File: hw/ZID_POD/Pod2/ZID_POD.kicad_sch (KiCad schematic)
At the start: 2 parts, among them J1 Z80-POD

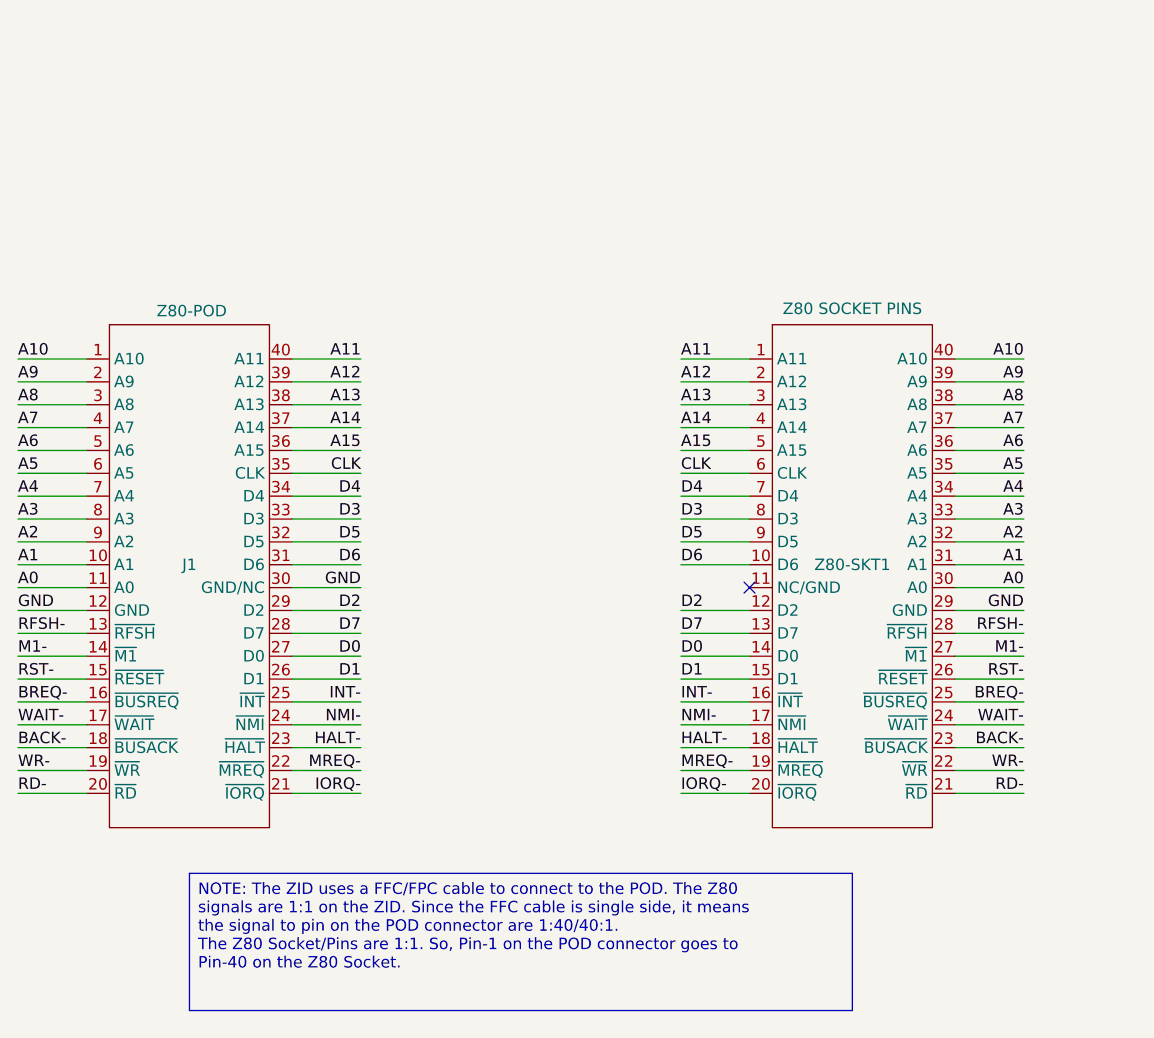
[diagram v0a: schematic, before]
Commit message: Change ZID,POD,ExpBP connector to SIP
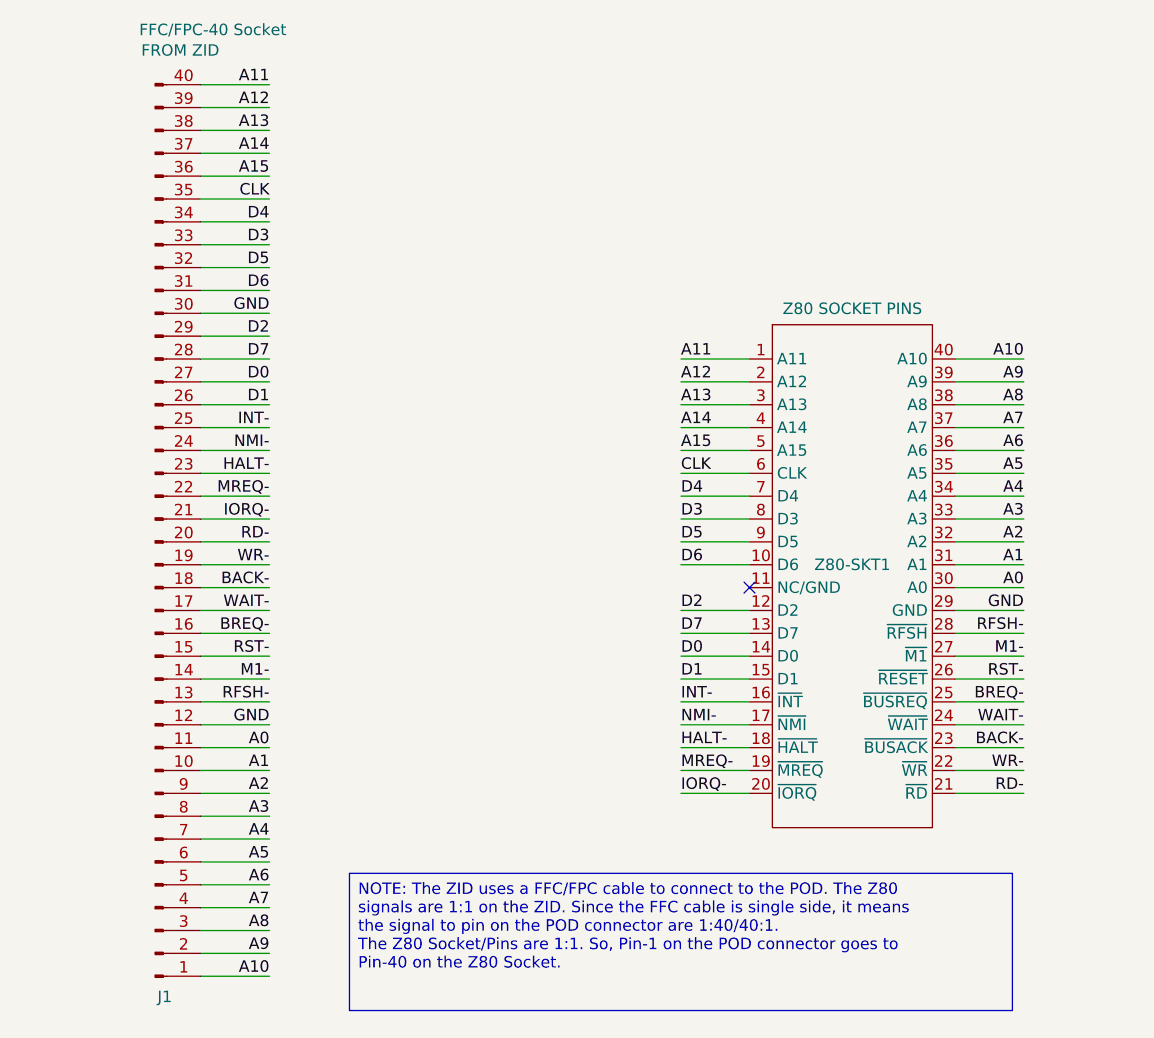
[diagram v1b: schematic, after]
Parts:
- removed J1: Z80-POD, AES_Library:CviLux_CF25401D0-05-NH_FFC-FPC-AES, symbol AES_Library:Z80-Pod-AES
- added J1: FFC/FPC-40 Socket, AES_Library:CviLux_CF25401D0-05-NH_FFC-FPC-AES, symbol Connector:Conn_01x40_Pin
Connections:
- net A0: now also J1.11 (Pin_11)
- net A1: now also J1.10 (Pin_10)
- net A10: now also J1.1 (Pin_1)
- net A11: now also J1.40 (Pin_40)
- net A12: now also J1.39 (Pin_39)
- net A13: now also J1.38 (Pin_38)
- net A14: now also J1.37 (Pin_37)
- net A15: now also J1.36 (Pin_36)
- net A2: now also J1.9 (Pin_9)
- net A3: now also J1.8 (Pin_8)
- net A4: now also J1.7 (Pin_7)
- net A5: now also J1.6 (Pin_6)
- net A6: now also J1.5 (Pin_5)
- net A7: now also J1.4 (Pin_4)
- net A8: now also J1.3 (Pin_3)
- net A9: now also J1.2 (Pin_2)
- net BACK-: now also J1.18 (Pin_18)
- net BREQ-: now also J1.16 (Pin_16)
- net CLK: now also J1.35 (Pin_35)
- net D0: now also J1.27 (Pin_27)
- net D1: now also J1.26 (Pin_26)
- net D2: now also J1.29 (Pin_29)
- net D3: now also J1.33 (Pin_33)
- net D4: now also J1.34 (Pin_34)
- net D5: now also J1.32 (Pin_32)
- net D6: now also J1.31 (Pin_31)
- net D7: now also J1.28 (Pin_28)
- net GND: now also J1.12 (Pin_12), J1.30 (Pin_30)
- net HALT-: now also J1.23 (Pin_23)
- net INT-: now also J1.25 (Pin_25)
- net IORQ-: now also J1.21 (Pin_21)
- net M1-: now also J1.14 (Pin_14)
- net MREQ-: now also J1.22 (Pin_22)
- net NMI-: now also J1.24 (Pin_24)
- net RD-: now also J1.20 (Pin_20)
- net RFSH-: now also J1.13 (Pin_13)
- net RST-: now also J1.15 (Pin_15)
- net WAIT-: now also J1.17 (Pin_17)
- net WR-: now also J1.19 (Pin_19)

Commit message: 74FCT541 to 74FCT2245. Move GND around CLK on ZID-POD connector
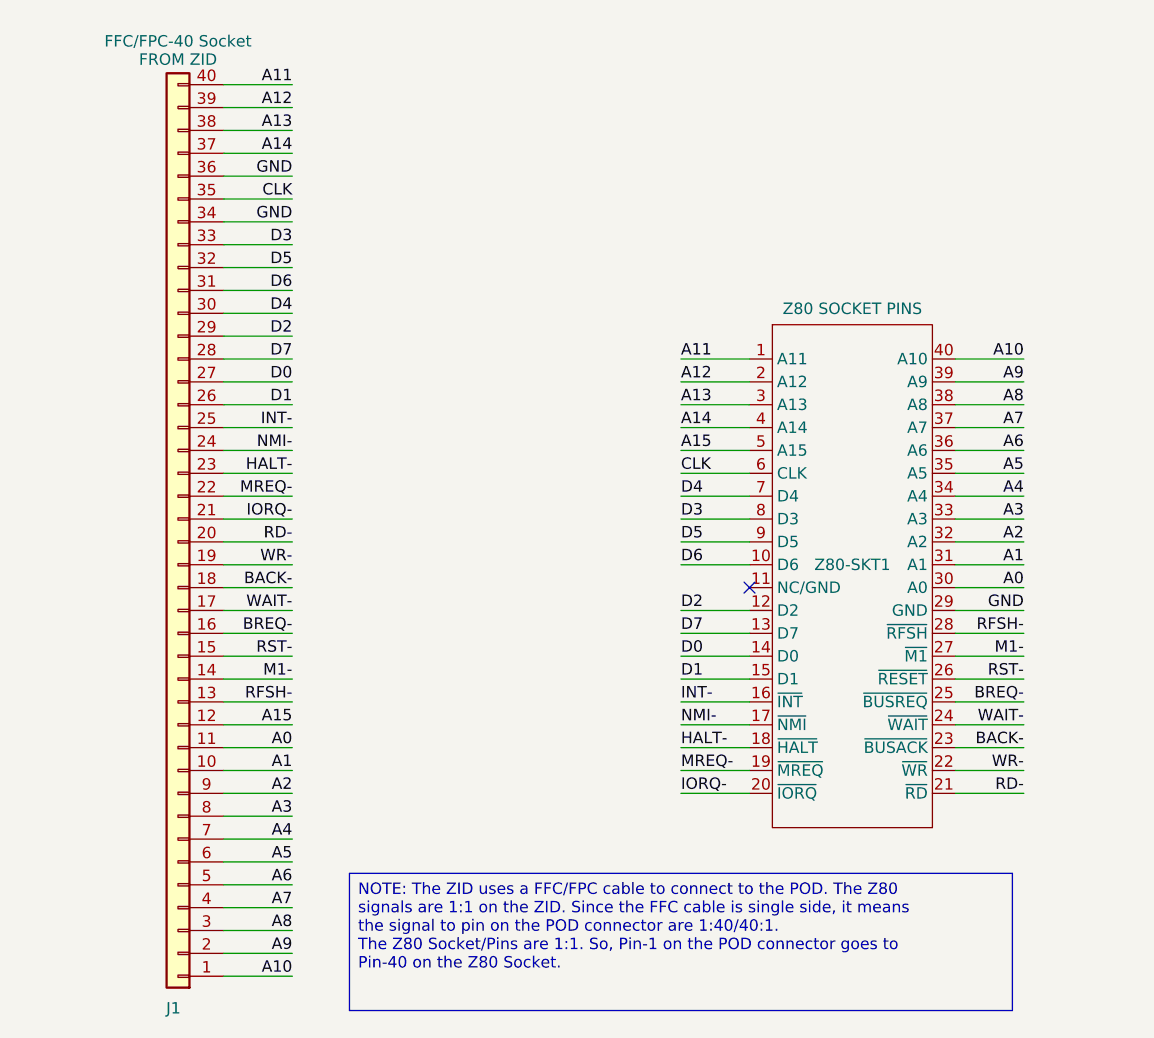
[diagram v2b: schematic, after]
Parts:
- removed J1: FFC/FPC-40 Socket, AES_Library:CviLux_CF25401D0-05-NH_FFC-FPC-AES, symbol Connector:Conn_01x40_Pin
- added J1: FFC/FPC-40 Socket, symbol Connector_Generic:Conn_01x40
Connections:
- net A0: now also J1.11 (Pin_11)
- net A1: now also J1.10 (Pin_10)
- net A10: now also J1.1 (Pin_1)
- net A11: now also J1.40 (Pin_40)
- net A12: now also J1.39 (Pin_39)
- net A13: now also J1.38 (Pin_38)
- net A14: now also J1.37 (Pin_37)
- net A15: now also J1.12 (Pin_12)
- net A2: now also J1.9 (Pin_9)
- net A3: now also J1.8 (Pin_8)
- net A4: now also J1.7 (Pin_7)
- net A5: now also J1.6 (Pin_6)
- net A6: now also J1.5 (Pin_5)
- net A7: now also J1.4 (Pin_4)
- net A8: now also J1.3 (Pin_3)
- net A9: now also J1.2 (Pin_2)
- net BACK-: now also J1.18 (Pin_18)
- net BREQ-: now also J1.16 (Pin_16)
- net CLK: now also J1.35 (Pin_35)
- net D0: now also J1.27 (Pin_27)
- net D1: now also J1.26 (Pin_26)
- net D2: now also J1.29 (Pin_29)
- net D3: now also J1.33 (Pin_33)
- net D4: now also J1.30 (Pin_30)
- net D5: now also J1.32 (Pin_32)
- net D6: now also J1.31 (Pin_31)
- net D7: now also J1.28 (Pin_28)
- net GND: now also J1.34 (Pin_34), J1.36 (Pin_36)
- net HALT-: now also J1.23 (Pin_23)
- net INT-: now also J1.25 (Pin_25)
- net IORQ-: now also J1.21 (Pin_21)
- net M1-: now also J1.14 (Pin_14)
- net MREQ-: now also J1.22 (Pin_22)
- net NMI-: now also J1.24 (Pin_24)
- net RD-: now also J1.20 (Pin_20)
- net RFSH-: now also J1.13 (Pin_13)
- net RST-: now also J1.15 (Pin_15)
- net WAIT-: now also J1.17 (Pin_17)
- net WR-: now also J1.19 (Pin_19)
